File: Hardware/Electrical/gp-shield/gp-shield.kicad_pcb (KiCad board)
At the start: 2 copper layers, 72.4 x 53.3 mm, 194 parts, among them J1 XT60/TERM2, J10 Conn_01x08, J11 Conn_01x04, J12 Conn_01x10, J13 T821-02x08, J14 Conn_01x04, J2 XT60/TERM2, J3 Conn_01x04, J4 Conn_01x03, J5 Conn_01x03, J6 Conn_01x03, J7 Conn_01x03, J8 Conn_01x03, J9 Conn_01x03, Q1 Q_PMOS_GDS, Q2 Q_PMOS_GDS, Q4 Q_PMOS_GDS, SW1 SW_SPDT, SW2 SW_Push, SW3 SW_Push, U1 NCP1117-5.0_SOT223, U3 LM397, U5 ADCMP350

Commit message: Added net classes
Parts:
- added C14: 100n, Capacitor_SMD:C_0805_2012Metric_Pad1.18x1.45mm_HandSolder, B.Cu at (119.4, 98.4)
- added C15: 100n, Capacitor_SMD:C_0805_2012Metric_Pad1.18x1.45mm_HandSolder, B.Cu at (123.2, 98.4)
- added L3: 22n, Inductor_SMD:L_0805_2012Metric_Pad1.15x1.40mm_HandSolder, B.Cu at (121.3, 98.4)
- F10, F11, F12, F13, F14, F15, F16, F17, F18, F19, F2, F20, F21, F22, F3, F4, F5, F6, F7, F8, F9: footprint Fuse:Fuse_0603_1608Metric_Pad1.05x0.95mm_HandSolder -> Fuse:Fuse_0805_2012Metric_Pad1.15x1.40mm_HandSolder
- moved SW1 28.1 mm to (47.3, 82.1), turned to 0 degrees
- moved C12 5.72 mm to (128.9, 98.4)
- moved C13 1.91 mm to (125.1, 98.4)
- moved J3 1.91 mm to (114.9, 78.1)
- moved L2 1.91 mm to (127.0, 98.4)
- moved kibuzzard-63527D9E 1.91 mm to (114.9, 82.5)
- moved kibuzzard-63527DAD 1.91 mm to (122.6, 82.5)
- moved kibuzzard-63527DBB 1.91 mm to (120.0, 82.5)
- moved kibuzzard-63527DC4 1.91 mm to (117.5, 82.5)
- moved kibuzzard-63527D35 1.27 mm to (118.7, 73.7)
- moved D20 0.64 mm to (145.4, 58.4)
- moved D26 0.64 mm to (138.4, 98.4)
- moved D13 0.64 mm to (116.2, 58.4)
- moved D10 0.63 mm to (130.2, 58.4)
- moved D12 0.63 mm to (135.3, 58.4)
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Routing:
- net GND: track 0.00 -> 11.3 mm, vias 0 -> 10
- net /MCU/A1: track 0.00 -> 6.11 mm
- net /MCU/A5: track 0.00 -> 6.11 mm
- net /MCU/A3: track 0.00 -> 6.11 mm
- net /MCU/D9: track 0.00 -> 6.06 mm
- net /MCU/D13: track 0.00 -> 6.06 mm
- net /MCU/D11: track 0.00 -> 6.06 mm
- net /MCU/D1: track 0.00 -> 5.96 mm
- net /MCU/D7: track 0.00 -> 5.96 mm
- net /MCU/D5: track 0.00 -> 5.96 mm
- net /MCU/D3: track 0.00 -> 5.96 mm
- net /IO/PWM.C1: track 28.3 -> 24.1 mm
- net /IO/PWM.B1: track 23.9 -> 26.5 mm
- net /IO/PWM.C0: track 33.1 -> 35.5 mm
- net /IO/PWM.B0: track 19.0 -> 21.3 mm
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- added copper zone on B.Cu, net GND
- added copper zone on F.Cu, net GND
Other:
- board text added: "All GPIO pins over-voltage and over-current protected."
- board text added: "gp-shield Rev. A A Marshall 2022"
- board text removed: "-"
- board text removed: "~"

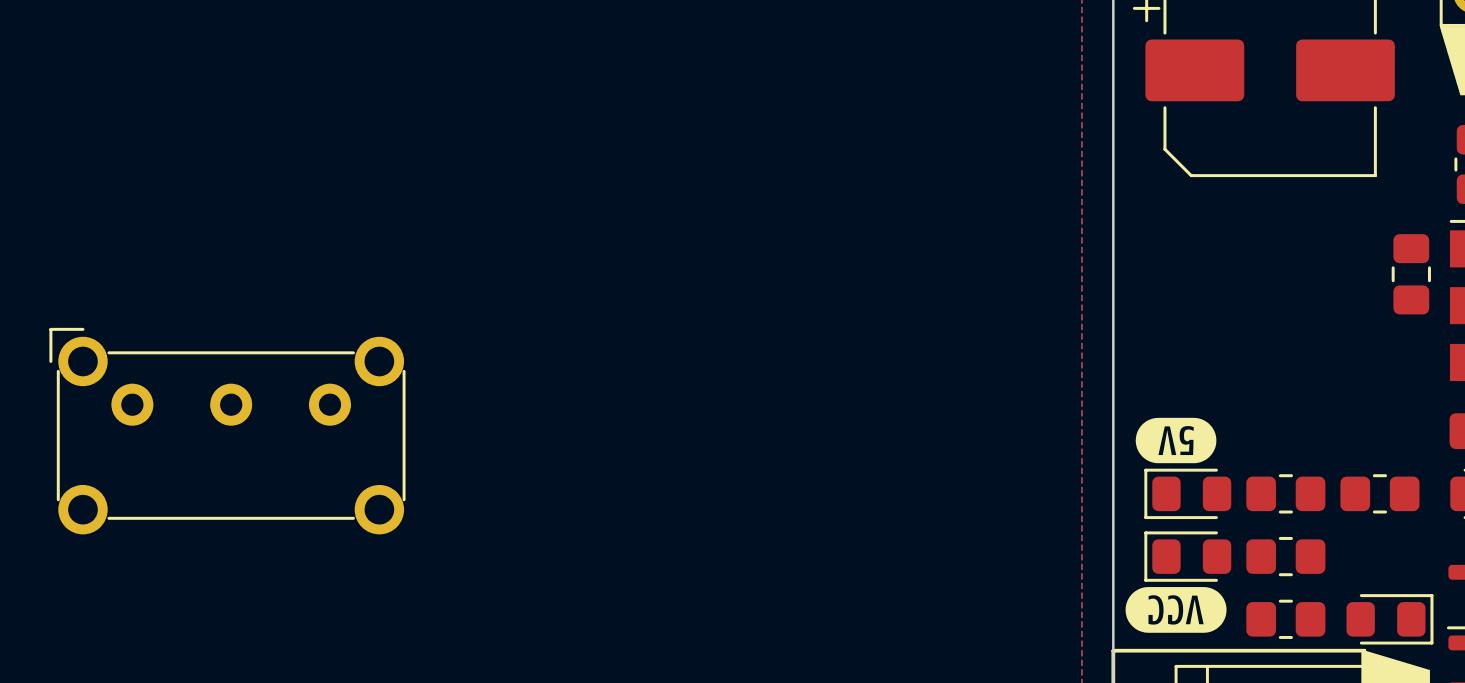
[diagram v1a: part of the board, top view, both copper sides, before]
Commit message: Updated PCB
- changed switch footprint
- created footprint library for E switch varieties
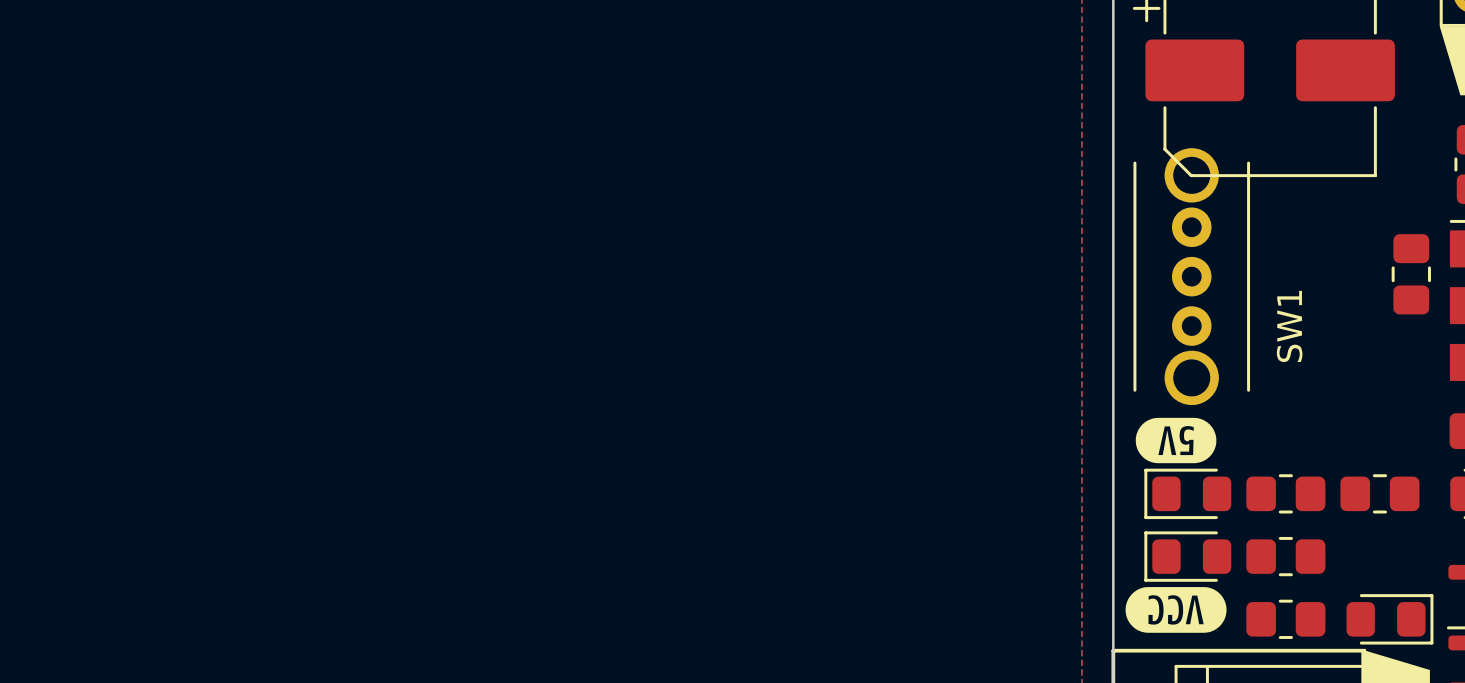
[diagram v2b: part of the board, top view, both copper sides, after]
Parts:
- SW1: footprint Button_Switch_THT:SW_E-Switch_EG1224_SPDT_Angled -> Utility:OS102011MA1_SPDT_ESwitch
- moved SW1 43.5 mm to (90.2, 74.9), turned to -90 degrees
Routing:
- net GND: track 11.3 -> 10.2 mm
- net /IO/ADC.AN0: track 26.4 -> 27.6 mm
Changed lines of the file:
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@@
     )
   )
+  (footprint "Utility:OS102011MA1_SPDT_ESwitch" (layer "F.Cu")
+    (at 90.17 74.93 -90)
+    (tags "switch SPDT")
+    (property "Sheetfile" "power.kicad_sch")
+    (property "Sheetname" "Power")
+    (attr through_hole)
+    (fp_text reference "SW1" (at 4 -4 90) (layer "F.SilkS")
+      (effects (font (size 1 1) (thickness 0.15)))
+    )
+    (fp_text value "SW_SPDT" (at 2.8 7.8 90) (layer "F.Fab")
+      (effects (font (size 1 1) (thickness 0.15)))
+    )
+    (fp_text user "${REFERENCE}" (at 4 1.25 90) (layer "F.Fab")
+      (effects (font (size 1 1) (thickness 0.1)))
+    )
+    (fp_line (start 6.6 2.3) (end -2.6 2.3) (layer "F.SilkS") (width 0.12))
+    (fp_line (start 6.6 -2.3) (end -2.6 -2.3) (layer "F.SilkS") (width 0.12))
+    (fp_line (start 7.4 -2.6) (end 7.4 2.8) (layer "F.CrtYd") (width 0.05))
+    (fp_line (start -3.4 2.8) (end -3.4 -2.6) (layer "F.CrtYd") (width 0.05))
+    (fp_line (start 7.4 2.8) (end 2.4 2.8) (layer "F.CrtYd") (width 0.05))
+    (fp_line (start 2.4 2.8) (end 2.4 6.6) (layer "F.CrtYd") (width 0.05))
+    (fp_line (start -3.4 -2.6) (end 7.4 -2.6) (layer "F.CrtYd") (width 0.05))
+    (fp_line (start -0.4 2.8) (end -3.4 2.8) (layer "F.CrtYd") (width 0.05))
+    (fp_line (start 2.4 6.6) (end -0.4 6.6) (layer "F.CrtYd") (width 0.05))
+    (fp_line (start -0.4 6.6) (end -0.4 2.8) (layer "F.CrtYd") (width 0.05))
+    (fp_line (start -2.6 2.2) (end -2.6 -2.2) (layer "F.Fab") (width 0.1))
+    (fp_line (start 6.6 2.2) (end -2.6 2.2) (layer "F.Fab") (width 0.1))
+    (fp_line (start 2 6.2) (end 2 2.2) (layer "F.Fab") (width 0.1))
+    (fp_line (start 0 2.2) (end 0 6.2) (layer "F.Fab") (width 0.1))
+    (fp_line (start 2 6.2) (end 0 6.2) (layer "F.Fab") (width 0.1))
+    (fp_line (start 6.6 -2.2) (end 6.6 2.2) (layer "F.Fab") (width 0.1))
+    (fp_line (start -2.6 -2.2) (end 6.6 -2.2) (layer "F.Fab") (width 0.1))
+    (pad "" thru_hole circle (at 6.1 0 270) (size 2.2 2.2) (drill 1.5) (layers *.Cu *.Mask))
+    (pad "" thru_hole circle (at -2.1 0 270) (size 2.2 2.2) (drill 1.5) (layers *.Cu *.Mask))
+    (pad "1" thru_hole circle (at 0 0 270) (size 1.6 1.6) (drill 0.8) (layers *.Cu *.Mask)
+      (net 86 "unconnected-(SW1-Pad1)") (pinfunction "A") (pintype "passive+no_connect"))
+    (pad "2" thru_hole circle (at 2 0 270) (size 1.6 1.6) (drill 0.8) (layers *.Cu *.Mask)
+      (net 74 "/Power/VCC_EN") (pinfunction "B") (pintype "passive"))
+    (pad "3" thru_hole circle (at 4 0 270) (size 1.6 1.6) (drill 0.8) (layers *.Cu *.Mask)
+      (net 75 "/Power/PWR_SW") (pinfunction "C") (pintype "passive"))
+  )
   (footprint "kibuzzard-63524FC9" (layer "F.Cu")
     (at 98.425 97.79 90)
@@
     )
   )
-  (footprint "Button_Switch_THT:SW_E-Switch_EG1224_SPDT_Angled" (layer "F.Cu")
-    (at 47.28 82.115)
-    (descr "E-Switch slide switch, EG series, SPDT, right angle, http://spec_sheets.e-switch.com/specs/P040042.pdf")
-    (tags "switch SPDT")
-    (property "Sheetfile" "power.kicad_sch")
-    (property "Sheetname" "Power")
-    (attr through_hole)
-    (fp_text reference "SW1" (at 4 -2.95) (layer "F.SilkS") hide
-      (effects (font (size 1 1) (thickness 0.15)))
-    )
-    (fp_text value "SW_SPDT" (at 4 14.45) (layer "F.Fab")
-      (effects (font (size 1 1) (thickness 0.15)))
-    )
-    (fp_text user "${REFERENCE}" (at 4 1.25) (layer "F.Fab") hide
-      (effects (font (size 1 1) (thickness 0.1)))
-    )
-    (fp_line (start -3 3.85) (end -3 -1.35) (layer "F.SilkS") (width 0.12))
-    (fp_line (start -3.3 -3.05) (end -2 -3.05) (layer "F.SilkS") (width 0.12))
-    (fp_line (start 8.95 4.6) (end -0.95 4.6) (layer "F.SilkS") (width 0.12))
-    (fp_line (start -0.95 -2.1) (end 8.95 -2.1) (layer "F.SilkS") (width 0.12))
-    (fp_line (start 11 -1.35) (end 11 3.85) (layer "F.SilkS") (width 0.12))
-    (fp_line (start -3.3 -1.75) (end -3.3 -3.05) (layer "F.SilkS") (width 0.12))
-    (fp_line (start -0.75 13.75) (end -0.75 5.5) (layer "F.CrtYd") (width 0.05))
-    (fp_line (start 11.25 5.5) (end 8.75 5.5) (layer "F.CrtYd") (width 0.05))
-    (fp_line (start -3.25 5.5) (end -3.25 -3) (layer "F.CrtYd") (width 0.05))
-    (fp_line (start -0.75 5.5) (end -3.25 5.5) (layer "F.CrtYd") (width 0.05))
-    (fp_line (start 8.75 5.5) (end 8.75 13.75) (layer "F.CrtYd") (width 0.05))
-    (fp_line (start 8.75 13.75) (end -0.75 13.75) (layer "F.CrtYd") (width 0.05))
-    (fp_line (start -3.25 -3) (end 11.25 -3) (layer "F.CrtYd") (width 0.05))
-    (fp_line (start 11.25 -3) (end 11.25 5.5) (layer "F.CrtYd") (width 0.05))
-    (fp_line (start -1.9 -2) (end -2.9 -1) (layer "F.Fab") (width 0.1))
-    (fp_line (start -0.5 13.5) (end -0.5 4.5) (layer "F.Fab") (width 0.1))
-    (fp_line (start -1.9 -2) (end 10.9 -2) (layer "F.Fab") (width 0.1))
-    (fp_line (start 4.5 13.5) (end -0.5 13.5) (layer "F.Fab") (width 0.1))
-    (fp_line (start 10.9 4.5) (end -2.9 4.5) (layer "F.Fab") (width 0.1))
-    (fp_line (start 10.9 -2) (end 10.9 4.5) (layer "F.Fab") (width 0.1))
-    (fp_line (start 4.5 4.5) (end 4.5 13.5) (layer "F.Fab") (width 0.1))
-    (fp_line (start -2.9 4.5) (end -2.9 -1) (layer "F.Fab") (width 0.1))
-    (pad "" thru_hole circle (at 10 -1.75) (size 2 2) (drill 1.2) (layers *.Cu *.Mask))
-    (pad "" thru_hole circle (at -2 -1.75) (size 2 2) (drill 1.2) (layers *.Cu *.Mask))
-    (pad "" thru_hole circle (at -2 4.25) (size 2 2) (drill 1.2) (layers *.Cu *.Mask))
-    (pad "" thru_hole circle (at 10 4.25) (size 2 2) (drill 1.2) (layers *.Cu *.Mask))
-    (pad "1" thru_hole circle (at 0 0) (size 1.7 1.7) (drill 0.9) (layers *.Cu *.Mask)
-      (net 86 "unconnected-(SW1-Pad1)") (pinfunction "A") (pintype "passive+no_connect"))
-    (pad "2" thru_hole circle (at 4 0) (size 1.7 1.7) (drill 0.9) (layers *.Cu *.Mask)
-      (net 74 "/Power/VCC_EN") (pinfunction "B") (pintype "passive"))
-    (pad "3" thru_hole circle (at 8 0) (size 1.7 1.7) (drill 0.9) (layers *.Cu *.Mask)
-      (net 75 "/Power/PWR_SW") (pinfunction "C") (pintype "passive"))
-    (model "${KICAD6_3DMODEL_DIR}/Button_Switch_THT.3dshapes/SW_E-Switch_EG1224_SPDT_Angled.wrl"
-      (offset (xyz 0 0 0))
-      (scale (xyz 1 1 1))
-      (rotate (xyz 0 0 0))
-    )
-  )
   (footprint "Connector_Molex:Molex_KK-254_AE-6410-04A_1x04_P2.54mm_Vertical" (layer "F.Cu")
     (at 114.935 78.105)
@@
   (segment (start 143.51 97.4) (end 143.51 96.266) (width 0.762) (layer "F.Cu") (net 5))
   (segment (start 121.285 59.445) (end 121.285 60.579) (width 0.762) (layer "F.Cu") (net 5))
-  (segment (start 138.43 97.4) (end 138.43 96.266) (width 0.762) (layer "F.Cu") (net 5))
   (segment (start 135.255 59.445) (end 135.255 60.579) (width 0.762) (layer "F.Cu") (net 5))
   (segment (start 130.175 59.445) (end 130.175 60.579) (width 0.762) (layer "F.Cu") (net 5))
@@
   (segment (start 113.665 59.295) (end 110.275 59.295) (width 0.254) (layer "F.Cu") (net 55))
   (segment (start 110.275 59.295) (end 104.14 65.43) (width 0.254) (layer "F.Cu") (net 55))
+  (segment (start 138.43 97.4) (end 138.43 96.266) (width 0.762) (layer "F.Cu") (net 57))
   (segment (start 139.7 80.0275) (end 145.4325 74.295) (width 0.254) (layer "B.Cu") (net 57))
   (segment (start 139.7 94.615) (end 139.7 80.0275) (width 0.254) (layer "B.Cu") (net 57))

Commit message: Major revisions
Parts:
- removed the C14 at (119.4, 98.4)
- removed the C15 at (123.2, 98.4)
- removed the C7 at (110.3, 71.8)
- removed the D3 at (98.0, 90.8)
- removed the D4 at (111.1, 87.0)
- removed the L3 at (121.3, 98.4)
- removed the Q1 at (102.2, 92.7)
- removed Q4: Q_PMOS_GDS, Package_TO_SOT_SMD:SOT-23
- removed the R1 at (105.4, 95.2)
- removed the R10 at (101.6, 72.4)
- removed R11: ?, Resistor_SMD:R_0805_2012Metric_Pad1.20x1.40mm_HandSolder
- removed the R14 at (110.5, 83.2)
- removed the R16 at (110.5, 79.4)
- removed the R2 at (94.0, 90.8)
- removed R7: 100K, Resistor_SMD:R_0805_2012Metric_Pad1.20x1.40mm_HandSolder
- removed U5: ADCMP350, Package_TO_SOT_SMD:Analog_KS-4
- added D2: D_Schottky, Diode_SMD:D_0805_2012Metric_Pad1.15x1.40mm_HandSolder, F.Cu at (101.6, 90.8)
- added D31: D_Schottky_Small, Diode_SMD:D_0805_2012Metric_Pad1.15x1.40mm_HandSolder, F.Cu at (128.3, 58.4)
- added D32: D_Schottky_Small, Diode_SMD:D_0805_2012Metric_Pad1.15x1.40mm_HandSolder, B.Cu at (147.3, 58.4)
- added D33: D_Schottky_Small, Diode_SMD:D_0805_2012Metric_Pad1.15x1.40mm_HandSolder, B.Cu at (151.1, 58.4)
- added D34: D_Schottky_Small, Diode_SMD:D_0805_2012Metric_Pad1.15x1.40mm_HandSolder, B.Cu at (124.5, 58.4)
- added D35: D_Schottky_Small, Diode_SMD:D_0805_2012Metric_Pad1.15x1.40mm_HandSolder, B.Cu at (128.3, 58.4)
- added D36: D_Schottky_Small, Diode_SMD:D_0805_2012Metric_Pad1.15x1.40mm_HandSolder, F.Cu at (141.0, 74.3)
- added D37: D_Schottky_Small, Diode_SMD:D_0805_2012Metric_Pad1.15x1.40mm_HandSolder, F.Cu at (141.0, 70.5)
- added D38: D_Schottky_Small, Diode_SMD:D_0805_2012Metric_Pad1.15x1.40mm_HandSolder, B.Cu at (139.1, 98.4)
- added D39: D_Schottky_Small, Diode_SMD:D_0805_2012Metric_Pad1.15x1.40mm_HandSolder, B.Cu at (135.3, 98.4)
- added D40: D_Schottky_Small, Diode_SMD:D_0805_2012Metric_Pad1.15x1.40mm_HandSolder, F.Cu at (139.0, 98.4)
- added D41: D_Schottky_Small, Diode_SMD:D_0805_2012Metric_Pad1.15x1.40mm_HandSolder, F.Cu at (135.3, 98.4)
- added D42: D_Schottky_Small, Diode_SMD:D_0805_2012Metric_Pad1.15x1.40mm_HandSolder, B.Cu at (144.8, 98.4)
- added D43: D_Schottky_Small, Diode_SMD:D_0805_2012Metric_Pad1.15x1.40mm_HandSolder, B.Cu at (141.0, 98.4)
- added D44: D_Schottky_Small, Diode_SMD:D_0805_2012Metric_Pad1.15x1.40mm_HandSolder, F.Cu at (144.7, 98.4)
- added D45: D_Schottky_Small, Diode_SMD:D_0805_2012Metric_Pad1.15x1.40mm_HandSolder, F.Cu at (141.0, 98.4)
- added D46: D_Schottky_Small, Diode_SMD:D_0805_2012Metric_Pad1.15x1.40mm_HandSolder, B.Cu at (150.5, 98.4)
- added D47: D_Schottky_Small, Diode_SMD:D_0805_2012Metric_Pad1.15x1.40mm_HandSolder, B.Cu at (146.7, 98.4)
- added D48: D_Schottky_Small, Diode_SMD:D_0805_2012Metric_Pad1.15x1.40mm_HandSolder, F.Cu at (150.5, 98.4)
- added D49: D_Schottky_Small, Diode_SMD:D_0805_2012Metric_Pad1.15x1.40mm_HandSolder, F.Cu at (146.7, 98.4)
- added D8: D_Schottky_Small, Diode_SMD:D_0805_2012Metric_Pad1.15x1.40mm_HandSolder, F.Cu at (130.2, 58.4)
- added D9: D_Schottky_Small, Diode_SMD:D_0805_2012Metric_Pad1.15x1.40mm_HandSolder, F.Cu at (134.0, 58.4)
- added JP1: Jumper_2_Open, Connector_PinHeader_2.54mm:PinHeader_1x02_P2.54mm_Vertical, F.Cu at (122.5, 109.9)
- added Q3: Q_NMOS_GDS, Package_TO_SOT_SMD:SOT-23, F.Cu at (124.1, 97.8)
- added R4: 100K, Resistor_SMD:R_0805_2012Metric_Pad1.20x1.40mm_HandSolder, F.Cu at (104.8, 80.0)
- added R9: 100K, Resistor_SMD:R_0805_2012Metric_Pad1.20x1.40mm_HandSolder, F.Cu at (107.3, 80.0)
- added RV1: R_Potentiometer, Potentiometer_SMD:Potentiometer_Bourns_3214W_Vertical, F.Cu at (109.2, 90.2)
- added U2: LM4040DBZ-2.5, Package_TO_SOT_SMD:SOT-23, F.Cu at (110.5, 80.0)
- C5: renamed from C8; footprint Capacitor_SMD:CP_Elec_8x5.4 -> Capacitor_THT:CP_Radial_D8.0mm_P3.50mm
- D10, D16, D17, D24, D26: value 5V1 -> D_Schottky_Small; moved to B.Cu
- D11, D12, D13, D18, D19, D20, D21, D25, D27, D28, D30: value 5V1 -> D_Schottky_Small
- D14, D15, D22, D23, D29: value 5V1 -> D_Schottky_Small; moved to F.Cu
- F1: footprint Fuse:Fuse_1812_4532Metric_Pad1.30x3.40mm_HandSolder -> Fuse:Fuse_Littelfuse-LVR100
- moved D30 46.7 mm to (124.5, 58.4), turned to -90 degrees
- moved D27 45.8 mm to (122.6, 58.4), turned to -90 degrees
- moved D26 44.6 mm to (118.7, 58.4), turned to -90 degrees
- moved D25 40.6 mm to (145.4, 58.4), turned to -90 degrees
- moved D28 40.2 mm to (147.3, 58.4), turned to -90 degrees
- moved D29 40.0 mm to (151.1, 58.4), turned to -90 degrees
- moved D18 30.5 mm to (113.0, 58.4)
- moved D22 29.8 mm to (118.7, 58.4)
- moved kibuzzard-635273DC 29.4 mm to (111.8, 102.9), turned to 90 degrees
- moved D6 25.6 mm to (111.8, 99.5), turned to 90 degrees
- moved D14 25.4 mm to (113.0, 58.4)
- moved D13 23.5 mm to (139.7, 58.4)
- moved R15 20.4 mm to (111.8, 95.6), turned to -90 degrees
- moved D21 19.0 mm to (145.4, 58.4)
- moved D17 18.4 mm to (139.7, 58.4)
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- renumbered C13 to C10, C16 to C11, C17 to C12, C18 to C13, C19 to C14, C20 to C15, C21 to C16, C22 to C17, C23 to C18, C24 to C19, C3 to C2, C25 to C20, C26 to C21, C27 to C22, C28 to C23, C29 to C24, C30 to C25, C31 to C26, C32 to C27, C33 to C28, C34 to C29, C5 to C3, C35 to C30, C9 to C6, C10 to C7, C11 to C8, C12 to C9, D2 to D1, D1 to D3, D5 to D4, D6 to D5, D8 to D6, D9 to D7, F9 to F10, F10 to F11, F11 to F12, F12 to F13, F13 to F14, F14 to F15, F15 to F16, F16 to F17, F17 to F18, F18 to F19, F19 to F20, F20 to F21, F21 to F22, F22 to F23, F2 to F3, F3 to F4, F4 to F5, F5 to F6, F6 to F7, F7 to F8, F8 to F9, L4 to L3, L5 to L4, L6 to L5, L7 to L6, L8 to L7, L9 to L8, Q2 to Q1, R3 to R1, R6 to R10, R12 to R14, R18 to R15, R19 to R16, R20 to R17, R21 to R18, R22 to R19, R4 to R2, R23 to R20, R5 to R3, U3 to U4
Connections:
- C2 pad 1: +5V_REG -> +5V
- C3 pad 1: /Power/+BATT_POL -> /Power/+BATT_FUSED
- C8 pad 1: Net-(C11-Pad1) -> /IO/PORTD4
- C9 pad 1: +5V -> /MCU/+5V_JMP
- D10 pad 1: /MCU/D7 -> +5V
- D10 pad 2: GND -> /MCU/D6
- D12 pad 1: /MCU/D5 -> +5V
- D12 pad 2: GND -> /MCU/D5
- D13 pad 1: /MCU/D13 -> /MCU/D5
- D14 pad 1: /MCU/D4 -> +5V
- D14 pad 2: GND -> /MCU/D13
- D15 pad 1: /MCU/D12 -> /MCU/D13
- D16 pad 1: /MCU/D3 -> +5V
- D16 pad 2: GND -> /MCU/D4
- D17 pad 1: /MCU/D11 -> /MCU/D4
- D18 pad 1: /MCU/D2 -> +5V
- D18 pad 2: GND -> /MCU/D12
- D19 pad 1: /MCU/D10 -> /MCU/D12
- D20 pad 1: /MCU/D1 -> +5V
- D20 pad 2: GND -> /MCU/D3
- D21 pad 1: /MCU/D9 -> /MCU/D3
- D22 pad 1: /MCU/D0 -> +5V
- D22 pad 2: GND -> /MCU/D11
- D23 pad 1: /MCU/D8 -> /MCU/D11
- D24 pad 1: /MCU/AREF -> +5V
- D24 pad 2: GND -> /MCU/D2
- D25 pad 1: /MCU/A0 -> /MCU/D2
- D26 pad 1: /MCU/A1 -> +5V
- D26 pad 2: GND -> /MCU/D10
- D27 pad 1: /MCU/A2 -> /MCU/D10
- D28 pad 1: /MCU/A3 -> +5V
- D28 pad 2: GND -> /MCU/D1
- D29 pad 1: /MCU/A4 -> /MCU/D1
- D3 pad 1: /Power/OVER_VOLT -> /Power/+BATT_FUSED
- D30 pad 1: /MCU/A5 -> +5V
- D30 pad 2: GND -> /MCU/D9
- D4 pad 1: /Power/+BATT_POL -> /Power/+BATT_FUSED
- D7 pad 1: GND -> /MCU/LED_OUT
- J3 pad 1: unconnected-(J3-Pad1) -> +5V
- J3 pad 2: unconnected-(J3-Pad2) -> /MCU/LED_OUT
- J3 pad 3: unconnected-(J3-Pad3) -> /IO/PORTD4
- J3 pad 4: unconnected-(J3-Pad4) -> GND
- L2 pad 2: +5V -> /MCU/+5V_JMP
- Q1 pad 3: /Power/+BATT_POL -> /Power/+BATT_FUSED
- R1 pad 1: /Power/+BATT_POL -> /Power/+BATT_FUSED
- R1 pad 2: /Power/VCC_CMP- -> /Power/VCC_CMP_POT+
- R10 pad 1: /Power/+BATT_POL -> /Power/+BATT_FUSED
- R16 pad 1: unconnected-(R19-Pad1) -> +5V
- R18 pad 1: Net-(C11-Pad1) -> /IO/PORTD4
- R2 pad 1: /Power/VCC_CMP- -> /Power/VCC_CMP_POT-
- R3 pad 1: /Power/+BATT_POL -> /Power/+BATT_FUSED
- R3 pad 2: /Power/VCC_CMP+ -> /Power/VCC_VREF
- SW1 pad 3: /Power/PWR_SW -> /Power/VCC_CMP_OUT
- U1 pad 2: +5V_REG -> +5V
- U4 pad 4: /Power/VCC_EN -> /Power/VCC_CMP_OUT
- U4 pad 5: /Power/+BATT_POL -> /Power/+BATT_FUSED
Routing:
- net +5V: track 0.00 -> 22.7 mm, vias 0 -> 10
- net GND: track 10.2 -> 22.6 mm
- net /IO/PORTB5: track 12.1 -> 0.00 mm
- net /IO/PORTB0: track 0.00 -> 12.0 mm
- net /IO/PORTB2: track 3.11 -> 14.5 mm
- net /IO/PORTB4: track 0.00 -> 10.7 mm
- net /IO/PORTD0: track 10.5 -> 20.1 mm
- net /MCU/D4: track 0.00 -> 9.22 mm
- net /MCU/D12: track 0.00 -> 9.03 mm
- net /MCU/D2: track 0.00 -> 8.95 mm
- net /MCU/D0: track 0.00 -> 8.87 mm
- net /MCU/D10: track 0.00 -> 8.77 mm
- net /MCU/D6: track 0.00 -> 8.69 mm
- net /MCU/D8: track 0.00 -> 8.32 mm
- net /IO/PORTD2: track 0.00 -> 7.56 mm
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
